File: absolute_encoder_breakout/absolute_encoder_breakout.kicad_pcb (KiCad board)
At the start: 2 copper layers, 10.2 x 9.1 mm, 4 parts, among them J1 Conn_01x03_Pin

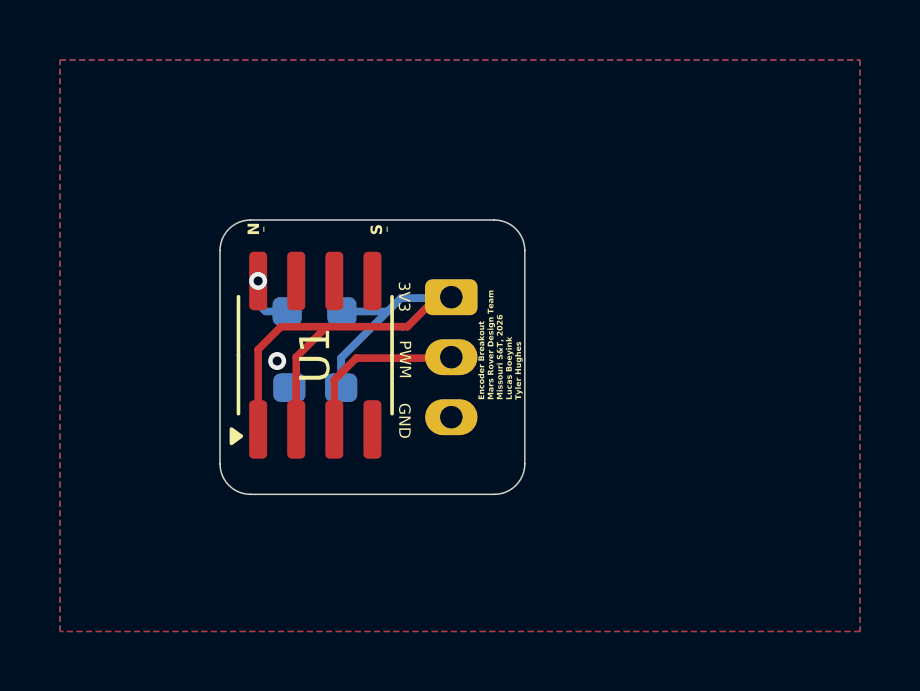
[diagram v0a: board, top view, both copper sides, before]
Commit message: Fix text size on encoder breakout
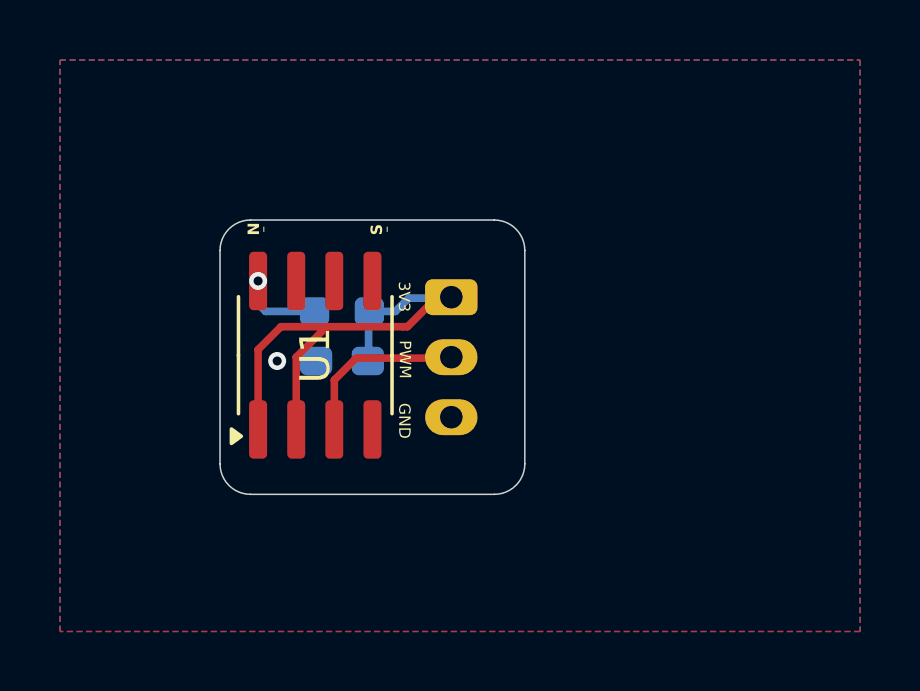
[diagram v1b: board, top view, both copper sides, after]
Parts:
- moved C1 1.26 mm to (140.2, 74.8)
- moved R1 0.91 mm to (140.2, 73.2)
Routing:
- net Net-(J1-Pin_1): track 19.7 -> 17.2 mm
- net Net-(U1-DIR): track 1.84 -> 2.75 mm
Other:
- board text added: "Encoder Brkout Rev1 2026 Lucas Boeyink Tyler Hughes"
- board text removed: "Encoder Breakout Mars Rover Design Team Missouri S&T, 2026 Lucas Boeyink Tyler Hughes"
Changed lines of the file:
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@@
 	(footprint "Resistor_SMD:R_0603_1608Metric_Pad0.98x0.95mm_HandSolder"
 		(layer "B.Cu")
-		(at 139.2955 73.152 180)
+		(at 140.208 73.152 180)
 		(descr "Resistor SMD 0603 (1608 Metric), square (rectangular) end terminal, IPC-7351 nominal with elongated pad for handsoldering. (Body size source: IPC-SM-782 page 72, https://www.pcb-3d.com/wordpress/wp-content/uploads/ipc-sm-782a_amendment_1_and_2.pdf), generated with kicad-footprint-generator")
 		(tags "resistor handsolder")
 		(property "Reference" "R1"
-			(at 0 1.524 0)
+			(at 2.667 0 0)
 			(layer "B.SilkS")
 			(effects
@@
 	(footprint "Capacitor_SMD:C_0603_1608Metric_Pad1.08x0.95mm_HandSolder"
 		(layer "B.Cu")
-		(at 139.319 75.692 180)
+		(at 140.208 74.803 180)
 		(descr "Capacitor SMD 0603 (1608 Metric), square (rectangular) end terminal, IPC-7351 nominal with elongated pad for handsoldering. (Body size source: IPC-SM-782 page 76, https://www.pcb-3d.com/wordpress/wp-content/uploads/ipc-sm-782a_amendment_1_and_2.pdf), generated with kicad-footprint-generator")
 		(tags "capacitor handsolder")
 		(property "Reference" "C1"
-			(at 0.0235 -1.498 0)
+			(at 2.54 0 180)
 			(layer "B.SilkS")
 			(effects
@@
 		)
 	)
-	(gr_text "Encoder Breakout\nMars Rover Design Team\nMissouri S&T, 2026\nLucas Boeyink\nTyler Hughes"
-		(at 146.2 76.1 90)
-		(layer "F.SilkS")
-		(effects
-			(font
-				(size 0.1905 0.1905)
-				(thickness 0.047625)
-				(bold yes)
-			)
-			(justify left bottom)
-		)
-	)
 	(gr_text "_\n"
 		(at 141.68 70.5 90)
@@
 			)
 			(justify left bottom)
+		)
+	)
+	(gr_text "Encoder Brkout\nRev1 2026\nLucas Boeyink\nTyler Hughes"
+		(at 142.113 78.74 0)
+		(layer "B.SilkS")
+		(effects
+			(font
+				(size 0.508 0.508)
+				(thickness 0.1016)
+				(bold yes)
+			)
+			(justify left bottom mirror)
 		)
 	)
@@
 	)
 	(segment
+		(start 137.414 72.898)
+		(end 137.414 72.136)
+		(width 0.254)
+		(layer "B.Cu")
+		(net 2)
+	)
+	(segment
+		(start 139.2955 73.152)
+		(end 137.668 73.152)
+		(width 0.254)
+		(layer "B.Cu")
+		(net 2)
+	)
+	(segment
 		(start 137.668 73.152)
 		(end 137.414 72.898)
-		(width 0.254)
-		(layer "B.Cu")
-		(net 2)
-	)
-	(segment
-		(start 137.414 72.898)
-		(end 137.414 72.136)
-		(width 0.254)
-		(layer "B.Cu")
-		(net 2)
-	)
-	(segment
-		(start 138.383 73.152)
-		(end 137.668 73.152)
 		(width 0.254)
 		(layer "B.Cu")
@@
 	)
 	(segment
-		(start 142.176 72.708)
-		(end 141.732 73.152)
+		(start 141.097 74.7765)
+		(end 141.097 73.1755)
 		(width 0.254)
 		(layer "B.Cu")
@@
 	(segment
 		(start 143.346 72.708)
-		(end 142.176 72.708)
-		(width 0.254)
-		(layer "B.Cu")
-		(net 6)
-	)
-	(segment
-		(start 140.1815 74.7025)
-		(end 140.1815 75.692)
-		(width 0.254)
-		(layer "B.Cu")
-		(net 6)
-	)
-	(segment
-		(start 141.732 73.152)
-		(end 140.1815 74.7025)
-		(width 0.254)
-		(layer "B.Cu")
-		(net 6)
-	)
-	(segment
-		(start 141.732 73.152)
-		(end 140.208 73.152)
-		(width 0.254)
-		(layer "B.Cu")
+		(end 142.43 72.708)
+		(width 0.254)
+		(layer "B.Cu")
+		(net 6)
+	)
+	(segment
+		(start 142.43 72.708)
+		(end 141.986 73.152)
+		(width 0.254)
+		(layer "B.Cu")
+		(net 6)
+	)
+	(segment
+		(start 141.097 73.1755)
+		(end 141.1205 73.152)
+		(width 0.254)
+		(layer "B.Cu")
+		(net 6)
+	)
+	(segment
+		(start 141.0705 74.803)
+		(end 141.097 74.7765)
+		(width 0.254)
+		(layer "B.Cu")
+		(net 6)
+	)
+	(segment
+		(start 141.986 73.152)
+		(end 141.1205 73.152)
+		(width 0.254)
+		(layer "B.Cu")
